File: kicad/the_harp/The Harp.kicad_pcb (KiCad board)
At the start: 4 copper layers, 56 x 94.5 mm, 17 parts, among them IC501 AK4621EF, J401 PJ-063AH, J402 NMJ6HCD2, SW101 100-DP6, SW102 100-DP6, SW103 100-DP6

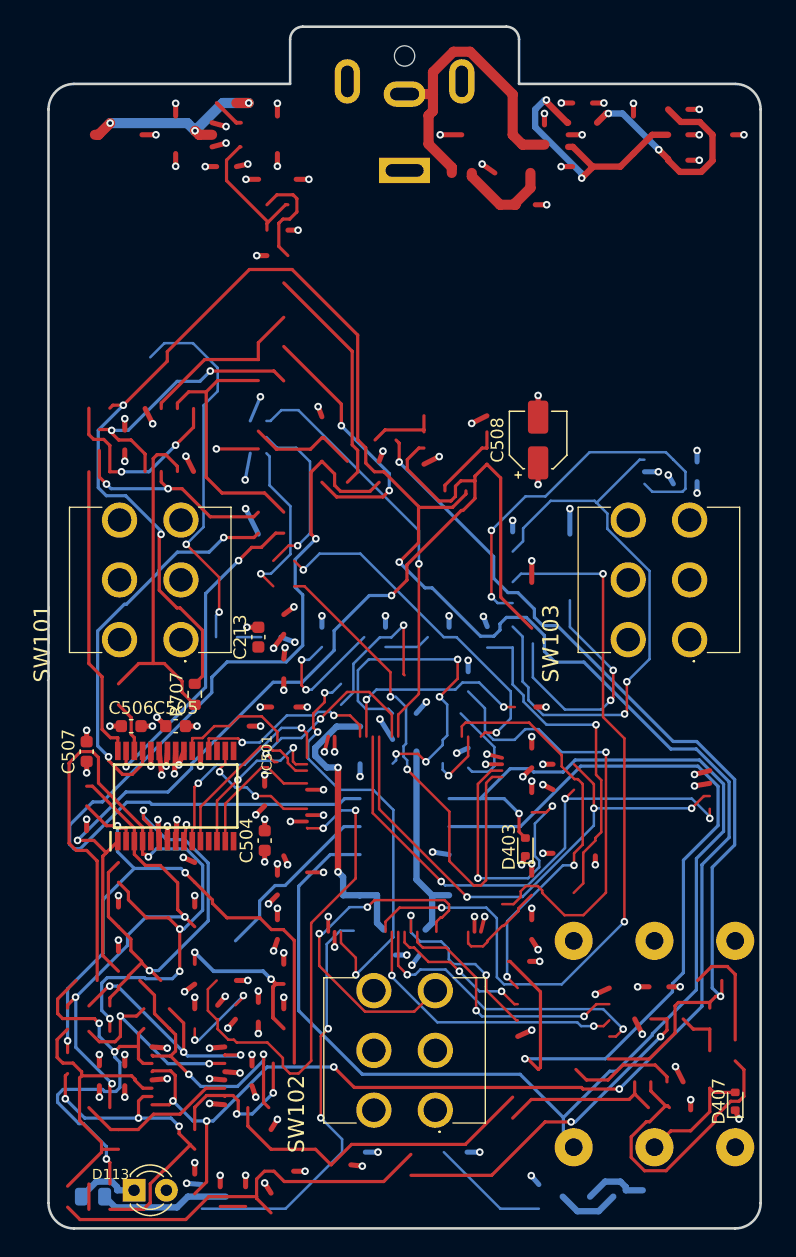
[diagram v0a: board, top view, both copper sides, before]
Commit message: Fix schematic load error and restore the board
KiCad 10 rejects (justify center): centre is the default and is not a
valid justify token. The generator (schgen._eff) now drops it, and the
266 occurrences are removed from the seven sub-sheets.

The pushed board (90ddafa) came from an Update PCB from Schematic run
while only part of the schematic loaded: it removed 164 footprints and
moved the tracks and vias onto unconnected or empty nets. The board is
restored from 53d04bc. The net class reordering in the project file is kept.

Co-Authored-By: Claude Opus 5.5 <noreply@anthropic.com>
Claude-Session: https://claude.ai/code/session_016hDejPHPgG8auBLMyByYZK
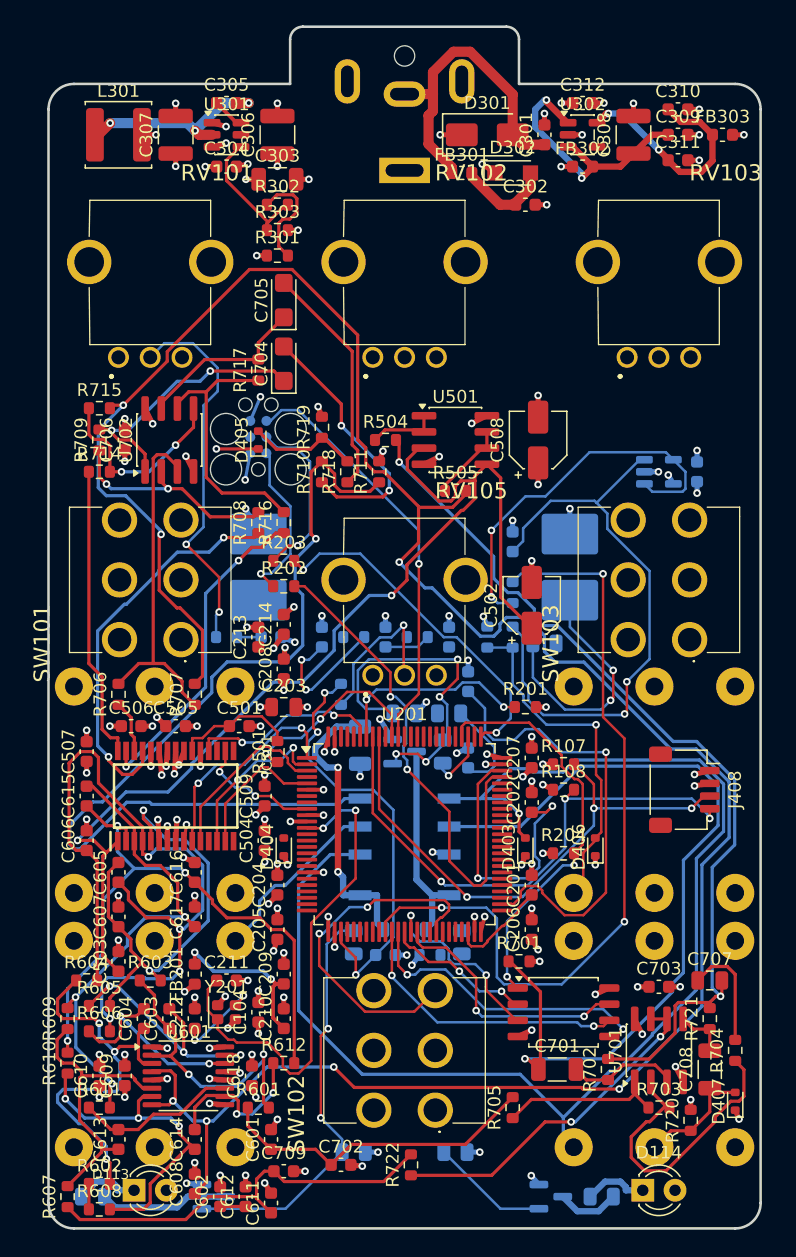
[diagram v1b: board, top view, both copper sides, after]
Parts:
- added C101: 100n, Capacitor_SMD:C_0603_1608Metric, B.Cu at (138.0, 96.5)
- added C102: 100n, Capacitor_SMD:C_0603_1608Metric, B.Cu at (142.0, 96.5)
- added C103: 100n, Capacitor_SMD:C_0603_1608Metric, B.Cu at (147.0, 96.5)
- added C104: 100n, Capacitor_SMD:C_0603_1608Metric, F.Cu at (137.0, 126.0)
- added C105: 100n, Capacitor_SMD:C_0603_1608Metric, B.Cu at (147.0, 121.5)
- added C201: 2.2u, Capacitor_SMD:C_0603_1608Metric, F.Cu at (158.5, 116.0)
- added C202: 2.2u, Capacitor_SMD:C_0603_1608Metric, F.Cu at (158.5, 109.5)
- added C203: 4.7u, Capacitor_SMD:C_0805_2012Metric, F.Cu at (139.0, 102.0)
- added C204: 100n, Capacitor_SMD:C_0603_1608Metric, F.Cu at (138.5, 116.0)
- added C205: 100n, Capacitor_SMD:C_0603_1608Metric, F.Cu at (138.5, 119.5)
- added C206: 100n, Capacitor_SMD:C_0603_1608Metric, F.Cu at (158.5, 119.5)
- added C207: 100n, Capacitor_SMD:C_0603_1608Metric, F.Cu at (158.5, 106.0)
- added C208: 100n, Capacitor_SMD:C_0603_1608Metric, F.Cu at (139.0, 99.0)
- added C209: 1u, Capacitor_SMD:C_0603_1608Metric, F.Cu at (139.0, 123.0)
- added C210: 100n, Capacitor_SMD:C_0603_1608Metric, F.Cu at (139.0, 126.5)
- added C211: 8p, Capacitor_SMD:C_0603_1608Metric, F.Cu at (134.5, 123.5)
- added C212: 8p, Capacitor_SMD:C_0603_1608Metric, F.Cu at (132.0, 126.5)
- added C214: 100n, Capacitor_SMD:C_0603_1608Metric, F.Cu at (139.0, 95.5)
- added C301: 2.2u, Capacitor_SMD:C_0603_1608Metric, F.Cu at (159.5, 57.0)
- added C302: 2.2u, Capacitor_SMD:C_0603_1608Metric, F.Cu at (158.0, 62.5)
- added C303: 10u, Capacitor_SMD:C_1206_3216Metric, F.Cu at (138.5, 60.5)
- added C304: 100n, Capacitor_SMD:C_0603_1608Metric, F.Cu at (134.5, 59.5)
- added C305: 100n, Capacitor_SMD:C_0603_1608Metric, F.Cu at (134.5, 54.5)
- added C306: 22u, Capacitor_SMD:C_1210_3225Metric, F.Cu at (138.5, 57.0)
- added C307: 22u, Capacitor_SMD:C_1210_3225Metric, F.Cu at (130.5, 57.0)
- added C308: 47u, Capacitor_SMD:C_1210_3225Metric, F.Cu at (166.5, 57.0)
- added C309: 2.2u, Capacitor_SMD:C_0603_1608Metric, F.Cu at (170.0, 57.0)
- added C310: 2.2u, Capacitor_SMD:C_0603_1608Metric, F.Cu at (170.0, 55.0)
- added C311: 2.2u, Capacitor_SMD:C_0603_1608Metric, F.Cu at (170.0, 59.0)
- added C312: 2.2u, Capacitor_SMD:C_0603_1608Metric, F.Cu at (162.5, 54.5)
- added C408: 100n, Capacitor_SMD:C_0603_1608Metric, B.Cu at (153.5, 106.0)
- added C409: 100n, Capacitor_SMD:C_0603_1608Metric, B.Cu at (153.5, 100.0)
- added C410: 100n, Capacitor_SMD:C_0603_1608Metric, B.Cu at (157.0, 89.0)
- added C411: 100n, Capacitor_SMD:C_0603_1608Metric, B.Cu at (171.5, 83.5)
- added C412: 2.7n, Capacitor_SMD:C_0603_1608Metric, B.Cu at (152.0, 96.5)
- added C501: 100n, Capacitor_SMD:C_0603_1608Metric, F.Cu at (135.5, 103.5)
- added C502: 10u, Capacitor_SMD:CP_Elec_4x5.8, F.Cu at (158.5, 94.0)
- added C503: 100n, Capacitor_SMD:C_0603_1608Metric, F.Cu at (126.0, 122.0)
- added C509: 100n, Capacitor_SMD:C_0603_1608Metric, F.Cu at (137.5, 109.0)
- added C601: 100p, Capacitor_SMD:C_0603_1608Metric, F.Cu at (138.0, 136.0)
- added C602: 100p, Capacitor_SMD:C_0603_1608Metric, F.Cu at (134.0, 140.5)
- added C603: 1n, Capacitor_SMD:C_0603_1608Metric, F.Cu at (130.0, 126.5)
- added C604: 1n, Capacitor_SMD:C_0603_1608Metric, F.Cu at (128.0, 126.5)
- added C605: 2.7n, Capacitor_SMD:C_0603_1608Metric, F.Cu at (126.0, 115.0)
- added C606: 100p, Capacitor_SMD:C_0603_1608Metric, F.Cu at (123.5, 112.5)
- added C607: 100p, Capacitor_SMD:C_0603_1608Metric, F.Cu at (126.0, 118.5)
- added C608: 100n, Capacitor_SMD:C_0603_1608Metric, F.Cu at (132.0, 139.5)
- added C609: 100n, Capacitor_SMD:C_0603_1608Metric, F.Cu at (126.5, 131.0)
- added C610: 100n, Capacitor_SMD:C_0603_1608Metric, F.Cu at (124.5, 131.0)
- added C611: 100p, Capacitor_SMD:C_0603_1608Metric, F.Cu at (138.0, 141.0)
- added C612: 100p, Capacitor_SMD:C_0603_1608Metric, F.Cu at (136.0, 140.5)
- added C613: 1n, Capacitor_SMD:C_0603_1608Metric, F.Cu at (126.0, 136.0)
- added C614: 1n, Capacitor_SMD:C_0603_1608Metric, F.Cu at (132.0, 136.0)
- added C615: 2.7n, Capacitor_SMD:C_0603_1608Metric, F.Cu at (123.5, 109.0)
- added C616: 100p, Capacitor_SMD:C_0603_1608Metric, F.Cu at (132.0, 115.0)
- added C617: 100p, Capacitor_SMD:C_0603_1608Metric, F.Cu at (132.0, 118.5)
- added C618: 100n, Capacitor_SMD:C_0603_1608Metric, F.Cu at (136.5, 131.0)
- added C701: 100n, Capacitor_SMD:C_1206_3216Metric, F.Cu at (160.5, 130.5)
- added C702: 220p, Capacitor_SMD:C_0603_1608Metric, F.Cu at (143.5, 138.0)
- added C703: 100n, Capacitor_SMD:C_0603_1608Metric, F.Cu at (168.5, 124.0)
- added C704: 10u, Capacitor_Tantalum_SMD:CP_EIA-3216-12_Kemet-S, F.Cu at (139.0, 75.0)
- added C705: 10u, Capacitor_Tantalum_SMD:CP_EIA-3216-12_Kemet-S, F.Cu at (139.0, 70.0)
- added C706: 100n, Capacitor_SMD:C_0603_1608Metric, F.Cu at (126.5, 81.0)
- added C707: 10u, Capacitor_SMD:C_0805_2012Metric, F.Cu at (172.5, 123.5)
- added C708: 100n, Capacitor_SMD:C_1206_3216Metric, F.Cu at (172.5, 130.5)
- added C709: 220p, Capacitor_SMD:C_0603_1608Metric, F.Cu at (139.0, 138.5)
- added D114: RED_LED, LED_THT:LED_D3.0mm, F.Cu at (167.2, 140.0)
- added D301: SMAJ10CA, Diode_SMD:D_SMA, F.Cu at (155.0, 57.0)
- added D302: PMEG3010ER, Diode_SMD:Nexperia_CFP3_SOD-123W, F.Cu at (157.0, 60.0)
- added D402: 1N4148W, Diode_SMD:D_SOD-123, B.Cu at (148.5, 119.5)
- added D404: PESD5V0U1BB,115, Diode_SMD:D_SOD-523, F.Cu at (139.0, 113.0)
- added D405: PESD5V0U1BB,115, Diode_SMD:D_SOD-523, F.Cu at (137.0, 81.0)
- added D406: PESD5V0U1BB,115, Diode_SMD:D_SOD-523, F.Cu at (163.5, 113.0)
- added FB201: 220R, Inductor_SMD:L_0603_1608Metric, F.Cu at (132.0, 123.0)
- added FB301: 600R, Inductor_SMD:L_0603_1608Metric, F.Cu at (153.0, 60.0)
- added FB302: 600R, Inductor_SMD:L_0603_1608Metric, F.Cu at (162.5, 59.5)
- added FB303: 600R, Inductor_SMD:L_0603_1608Metric, F.Cu at (173.5, 57.0)
- added J403: NMJ6HCD2, Connector_Audio:Jack_6.35mm_Neutrik_NMJ6HCD2_Horizontal, B.Cu at (135.2, 120.4)
- added J404: NMJ6HCD2, Connector_Audio:Jack_6.35mm_Neutrik_NMJ6HCD2_Horizontal, B.Cu at (135.2, 100.4)
- added J405: Bypass FSW, Resistor_SMD:R_2816_7142Metric_Pad3.20x4.45mm_HandSolder, B.Cu at (137.0, 91.0)
- added J406: NMJ6HCD2, Connector_Audio:Jack_6.35mm_Neutrik_NMJ6HCD2_Horizontal, B.Cu at (161.8, 116.6)
- added J407: Hold FSW, Resistor_SMD:R_2816_7142Metric_Pad3.20x4.45mm_HandSolder, B.Cu at (161.5, 91.0)
- added J408: OLED 0.91 128x32, Connector_JST:JST_SH_SM04B-SRSS-TB_1x04-1MP_P1.00mm_Horizontal, F.Cu at (170.5, 108.5)
- added K401: G6K-2F-Y, Relay_SMD:Relay_DPDT_Omron_G6K-2F-Y, B.Cu at (148.5, 113.0)
- added L301: 10u, Inductor_SMD:L_APV_ANR5020, F.Cu at (126.0, 57.0)
- added Q401: 2N7002, Package_TO_SOT_SMD:SOT-23, B.Cu at (148.5, 105.5)
- added Q402: 2N7002, Package_TO_SOT_SMD:SOT-23, B.Cu at (133.5, 140.5)
- added Q403: 2N7002, Package_TO_SOT_SMD:SOT-23, B.Cu at (160.0, 140.5)
- added R101: 1k, Resistor_SMD:R_0603_1608Metric, B.Cu at (134.5, 96.5)
- added R102: 1k, Resistor_SMD:R_0603_1608Metric, B.Cu at (144.5, 96.5)
- added R103: 1k, Resistor_SMD:R_0603_1608Metric, B.Cu at (149.5, 96.5)
- added R105: 1k, Resistor_SMD:R_0603_1608Metric, B.Cu at (143.5, 101.0)
- added R107: 4.7k, Resistor_SMD:R_0603_1608Metric, F.Cu at (161.0, 106.5)
- added R108: 4.7k, Resistor_SMD:R_0603_1608Metric, F.Cu at (161.0, 108.5)
- added R201: 10k, Resistor_SMD:R_0603_1608Metric, F.Cu at (158.0, 102.0)
- added R202: 22R, Resistor_SMD:R_0603_1608Metric, F.Cu at (139.0, 92.5)
- added R203: 22R, Resistor_SMD:R_0603_1608Metric, F.Cu at (139.0, 90.5)
- added R204: 10k, Resistor_SMD:R_0603_1608Metric, F.Cu at (161.0, 113.5)
- added R301: 49.9, Resistor_SMD:R_0603_1608Metric, F.Cu at (138.5, 66.5)
- added R302: 100k, Resistor_SMD:R_0603_1608Metric, F.Cu at (138.5, 62.5)
- added R303: 22k, Resistor_SMD:R_0603_1608Metric, F.Cu at (138.5, 64.5)
- added R405: 150R, Resistor_SMD:R_1206_3216Metric, B.Cu at (145.0, 105.0)
- added R406: 100R, Resistor_SMD:R_0805_2012Metric, B.Cu at (151.5, 105.5)
- added R407: 100k, Resistor_SMD:R_0805_2012Metric, B.Cu at (148.5, 102.5)
- added R408: 100R, Resistor_SMD:R_0805_2012Metric, B.Cu at (144.5, 120.5)
- added R409: 100k, Resistor_SMD:R_0805_2012Metric, B.Cu at (144.5, 137.0)
- added R410: 1k, Resistor_SMD:R_0805_2012Metric, B.Cu at (152.0, 102.5)
- added R411: 1k, Resistor_SMD:R_0805_2012Metric, B.Cu at (164.0, 140.5)
- added R412: 100R, Resistor_SMD:R_0805_2012Metric, B.Cu at (153.0, 120.5)
- added R413: 100k, Resistor_SMD:R_0805_2012Metric, B.Cu at (152.5, 137.0)
- added R414: 1k, Resistor_SMD:R_0805_2012Metric, B.Cu at (159.5, 97.0)
- added R415: 100R, Resistor_SMD:R_0603_1608Metric, B.Cu at (150.5, 121.5)
- added R416: 1k, Resistor_SMD:R_0603_1608Metric, B.Cu at (157.0, 96.5)
- added R417: 100k, Resistor_SMD:R_0603_1608Metric, B.Cu at (155.0, 96.5)
- added R418: 100R, Resistor_SMD:R_0603_1608Metric, B.Cu at (157.0, 93.0)
- added R501: 5k1, Resistor_SMD:R_0603_1608Metric, F.Cu at (138.5, 105.5)
- added R504: 10R, Resistor_SMD:R_0603_1608Metric, F.Cu at (147.0, 81.0)
- added R505: 10R, Resistor_SMD:R_0603_1608Metric, F.Cu at (152.5, 85.0)
- added R601: 1k, Resistor_SMD:R_0603_1608Metric, F.Cu at (137.0, 133.5)
- added R602: 1.05k, Resistor_SMD:R_0603_1608Metric, F.Cu at (124.5, 139.5)
- added R603: 620, Resistor_SMD:R_0603_1608Metric, F.Cu at (128.5, 123.5)
- added R604: 620, Resistor_SMD:R_0603_1608Metric, F.Cu at (123.5, 123.5)
- added R605: 40.2, Resistor_SMD:R_0603_1608Metric, F.Cu at (124.5, 125.5)
- added R606: 40.2, Resistor_SMD:R_0603_1608Metric, F.Cu at (124.5, 127.5)
- added R607: 1k, Resistor_SMD:R_0603_1608Metric, F.Cu at (122.0, 140.5)
- added R608: 1.05k, Resistor_SMD:R_0603_1608Metric, F.Cu at (124.5, 141.5)
- added R609: 620, Resistor_SMD:R_0603_1608Metric, F.Cu at (122.0, 126.5)
- added R610: 620, Resistor_SMD:R_0603_1608Metric, F.Cu at (122.0, 130.0)
- added R611: 40.2, Resistor_SMD:R_0603_1608Metric, F.Cu at (124.5, 133.5)
- added R612: 40.2, Resistor_SMD:R_0603_1608Metric, F.Cu at (139.0, 130.0)
- added R701: 1M, Resistor_SMD:R_0603_1608Metric, F.Cu at (157.5, 122.0)
- added R702: 1M, Resistor_SMD:R_0603_1608Metric, F.Cu at (164.5, 130.5)
- added R703: 0R, Resistor_SMD:R_0603_1608Metric, F.Cu at (168.5, 133.5)
- added R704: 0R, Resistor_SMD:R_0603_1608Metric, F.Cu at (174.5, 129.0)
- added R705: 49.9, Resistor_SMD:R_0603_1608Metric, F.Cu at (157.0, 133.5)
- added R706: 10k, Resistor_SMD:R_0603_1608Metric, F.Cu at (126.0, 101.0)
- added R708: 10k, Resistor_SMD:R_0603_1608Metric, F.Cu at (137.0, 87.5)
- added R709: 10k, Resistor_SMD:R_0603_1608Metric, F.Cu at (124.5, 81.0)
- added R710: 100R, Resistor_SMD:R_0603_1608Metric, F.Cu at (142.0, 83.5)
- added R711: 1M, Resistor_SMD:R_0603_1608Metric, F.Cu at (146.5, 83.5)
- added R714: 10k, Resistor_SMD:R_0603_1608Metric, F.Cu at (124.5, 83.5)
- added R715: 10k, Resistor_SMD:R_0603_1608Metric, F.Cu at (124.5, 78.5)
- added R716: 10k, Resistor_SMD:R_0603_1608Metric, F.Cu at (139.0, 87.5)
- added R717: 10k, Resistor_SMD:R_0603_1608Metric, F.Cu at (137.0, 75.5)
- added R718: 100R, Resistor_SMD:R_0603_1608Metric, F.Cu at (144.0, 83.5)
- added R719: 1M, Resistor_SMD:R_0603_1608Metric, F.Cu at (142.0, 80.0)
- added R720: 1M, Resistor_SMD:R_0603_1608Metric, F.Cu at (171.0, 134.5)
- added R721: 1M, Resistor_SMD:R_0603_1608Metric, F.Cu at (172.5, 126.5)
- added R722: 49.9, Resistor_SMD:R_0603_1608Metric, F.Cu at (149.0, 138.0)
- added RV101: B10K, Potentiometer_THT:RD901F4015R1B10K00DL1, F.Cu at (126.0, 74.5)
- added RV102: B10K, Potentiometer_THT:RD901F4015R1B10K00DL1, F.Cu at (146.0, 74.5)
- added RV103: B10K, Potentiometer_THT:RD901F4015R1B10K00DL1, F.Cu at (166.0, 74.5)
- added RV105: B10K, Potentiometer_THT:RD901F4015R1B10K00DL1, F.Cu at (146.0, 99.5)
- added U201: STM32H750VBT6, Package_QFP:LQFP-100_14x14mm_P0.5mm, F.Cu at (148.5, 112.0)
- added U202: W25Q128JVSIQ, Package_SO:SOIC-8_5.23x5.23mm_P1.27mm, F.Cu at (161.0, 126.0)
- added U301: TPS54202DDC, Package_TO_SOT_SMD:SOT-23-6, F.Cu at (134.5, 57.0)
- added U302: NCP718ASN500T1G, Package_TO_SOT_SMD:TSOT-23-5, F.Cu at (162.5, 57.0)
- added U401: MCP6001T-I/OT, Package_TO_SOT_SMD:SOT-23-5, B.Cu at (168.5, 83.5)
- added U501: OPA2348AIDR, Package_SO:SOIC-8_3.9x4.9mm_P1.27mm, F.Cu at (152.5, 81.0)
- added U601: THS4522IPW, Package_SO:TSSOP-16_4.4x5mm_P0.65mm, F.Cu at (131.5, 131.0)
- added U701: OPA2365AIDR, Package_SO:SOIC-8_3.9x4.9mm_P1.27mm, F.Cu at (168.5, 129.0)
- added U702: OPA1688IDR, Package_SO:SOIC-8_3.9x4.9mm_P1.27mm, F.Cu at (130.0, 81.0)
- added W201: SWD needle, LIB_STLINK:SEGGER_8.06.05_6-PIN_NEEDLE_ADAPTER, B.Cu at (137.0, 79.5)
- added Y201: 25MHz 9pF, Crystal:Crystal_SMD_2016-4Pin_2.0x1.6mm, F.Cu at (134.5, 126.0)
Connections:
- C213 pad 1: unconnected-(C213-Pad1) -> /MCU/NRST
- C213 pad 2: unconnected-(C213-Pad2) -> GND
- C504 pad 1: unconnected-(C504-Pad1) -> +3V3
- C504 pad 2: unconnected-(C504-Pad2) -> GND
- C505 pad 1: unconnected-(C505-Pad1) -> +3V3
- C505 pad 2: unconnected-(C505-Pad2) -> GND
- C506 pad 1: unconnected-(C506-Pad1) -> +3V3
- C506 pad 2: unconnected-(C506-Pad2) -> GND
- C507 pad 1: unconnected-(C507-Pad1) -> +5V
- C507 pad 2: unconnected-(C507-Pad2) -> GND
- C508 pad 1: unconnected-(C508-Pad1) -> +5V
- C508 pad 2: unconnected-(C508-Pad2) -> GND
- D113 pad 1: unconnected-(D113-K-Pad1) -> /Jacks and Bypass/LED_EFF_K
- D113 pad 2: unconnected-(D113-A-Pad2) -> +9V
- D403 pad 1: unconnected-(D403-A1-Pad1) -> GND
- D403 pad 2: unconnected-(D403-A2-Pad2) -> /Jacks and Bypass/IN
- D407 pad 1: unconnected-(D407-A1-Pad1) -> GND
- D407 pad 2: unconnected-(D407-A2-Pad2) -> IN_R
- IC501 pad 1: unconnected-(IC501-VCOM-Pad1) -> /Codec/VCOM
- IC501 pad 10: unconnected-(IC501-MCLK-Pad10) -> CODEC_MCLK
- IC501 pad 11: unconnected-(IC501-LRCK-Pad11) -> CODEC_LRCK
- IC501 pad 12: unconnected-(IC501-BICK-Pad12) -> CODEC_BICK
- IC501 pad 13: unconnected-(IC501-SDTO-Pad13) -> CODEC_SDTO
- IC501 pad 14: unconnected-(IC501-SDTI-Pad14) -> CODEC_SDTI
- IC501 pad 17: unconnected-(IC501-CDTI/CKS0-Pad17) -> CODEC_CDTI
- IC501 pad 18: unconnected-(IC501-CCLK/CKS1-Pad18) -> CODEC_CCLK
- IC501 pad 19: unconnected-(IC501-CSN/DIF-Pad19) -> CODEC_CSN
- IC501 pad 2: unconnected-(IC501-AINR+-Pad2) -> ADC_R_P
- IC501 pad 20: unconnected-(IC501-DFS0-Pad20) -> GND
- IC501 pad 21: unconnected-(IC501-PDN-Pad21) -> /Codec/PDN
- IC501 pad 22: unconnected-(IC501-DEM0-Pad22) -> GND
- IC501 pad 23: unconnected-(IC501-SDFIL-Pad23) -> GND
- IC501 pad 24: unconnected-(IC501-TVDD-Pad24) -> +3V3
- IC501 pad 25: unconnected-(IC501-DVDD-Pad25) -> +3V3
- IC501 pad 26: unconnected-(IC501-VSS2-Pad26) -> GND
- IC501 pad 27: unconnected-(IC501-AOUTL--Pad27) -> DAC_L_N
- IC501 pad 28: unconnected-(IC501-AOUTL+-Pad28) -> DAC_L_P
- IC501 pad 29: unconnected-(IC501-AOUTR--Pad29) -> DAC_R_N
- IC501 pad 3: unconnected-(IC501-AINR--Pad3) -> ADC_R_N
- IC501 pad 30: unconnected-(IC501-AOUTR+-Pad30) -> DAC_R_P
- IC501 pad 4: unconnected-(IC501-AINL+-Pad4) -> ADC_L_P
- IC501 pad 5: unconnected-(IC501-AINL--Pad5) -> ADC_L_N
- IC501 pad 6: unconnected-(IC501-VREF-Pad6) -> +5V
- IC501 pad 7: unconnected-(IC501-VSS1-Pad7) -> GND
- IC501 pad 8: unconnected-(IC501-AVDD-Pad8) -> +5V
- IC501 pad 9: unconnected-(IC501-P/S-Pad9) -> +3V3
- J402 pad R: unconnected-(J402-PadR) -> IN_R
- J402 pad S: unconnected-(J402-PadS) -> GND
- J402 pad T: unconnected-(J402-PadT) -> /Jacks and Bypass/IN
- R404 pad 1: unconnected-(R404-Pad1) -> /Jacks and Bypass/LED_EFF_K
- R404 pad 2: unconnected-(R404-Pad2) -> /Jacks and Bypass/LED_EFF_LOW
- R707 pad 1: unconnected-(R707-Pad1) -> /Analog In and Out/OUTL_P
- R707 pad 2: unconnected-(R707-Pad2) -> VCOM_B
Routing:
- net (no net): track 2254.0 -> 0.00 mm, vias 151 -> 0
- net +3V3: track 0.00 -> 310.7 mm, vias 0 -> 34
- net unconnected-(D113-A-Pad2): track 238.1 -> 0.00 mm, vias 6 -> 0
- net +9V: track 0.00 -> 238.1 mm, vias 0 -> 6
- net +5V: track 0.00 -> 198.6 mm, vias 0 -> 19
- net VCOM_B: track 0.00 -> 192.7 mm, vias 0 -> 7
- net unconnected-(R707-Pad2): track 192.7 -> 0.00 mm, vias 7 -> 0
- net /Jacks and Bypass/IN: track 0.00 -> 103.9 mm, vias 0 -> 1
- net unconnected-(IC501-VCOM-Pad1): track 85.5 -> 0.00 mm, vias 2 -> 0
- net /Codec/VCOM: track 0.00 -> 85.5 mm, vias 0 -> 2
- net VCOM_A: track 0.00 -> 75.9 mm, vias 0 -> 2
- net EFFECT_OUT_L: track 0.00 -> 73.4 mm, vias 0 -> 1
- net EFFECT_IN: track 0.00 -> 66.3 mm, vias 0 -> 1
- net EXP: track 0.00 -> 62.7 mm, vias 0 -> 3
- net ADC_L_P: track 0.00 -> 62.6 mm, vias 0 -> 4
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- added copper zone on In1.Cu, net GND
- removed copper zone on In1.Cu, net unconnected-(J402-PadS)
